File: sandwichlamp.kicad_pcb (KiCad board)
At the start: 2 copper layers, 96 x 96 mm, 17 parts, among them J1 Conn_01x01_Pin, J2 Conn_01x01_Pin, J3 Conn_01x01_Pin, J4 12V Enable, J5 HLK-LD2410C, J6 Conn_01x20_Pin, SW1 SW_SPDT, U1 magnetic-charger, U3 hw357, U4 RX480E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

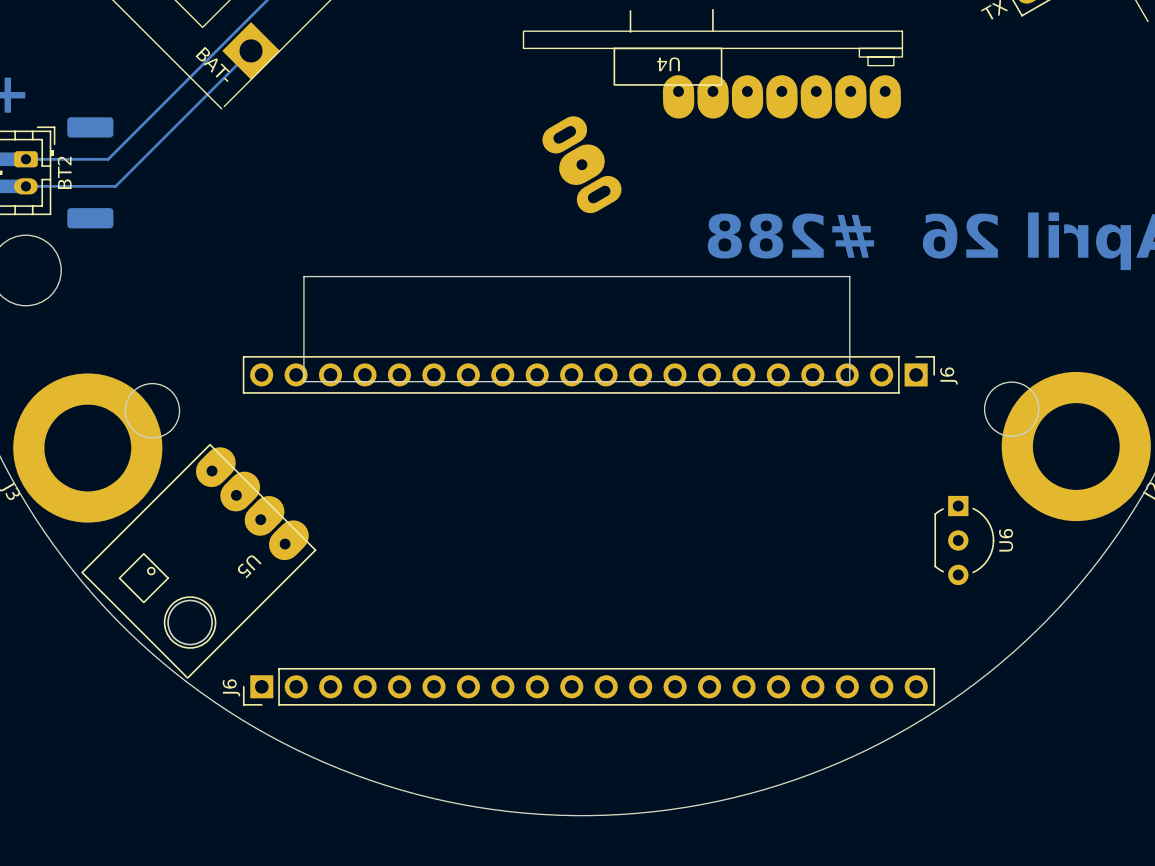
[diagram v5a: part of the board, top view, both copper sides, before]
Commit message: Add the new Lolin32 footprint
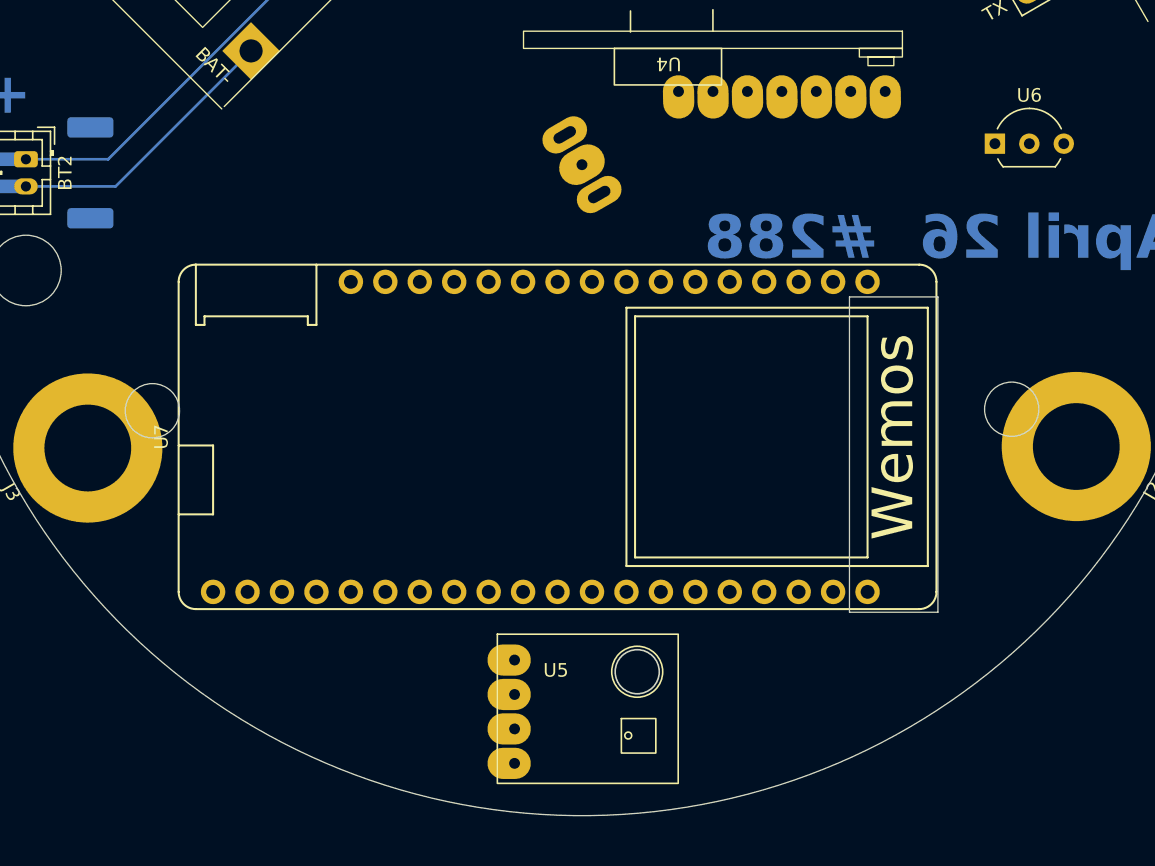
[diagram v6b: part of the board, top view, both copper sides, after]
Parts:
- removed J6 (x2): Conn_01x20_Pin, Connector_PinHeader_2.54mm:PinHeader_1x20_P2.54mm_Vertical
- added U7: Lolin32, lolin32:lolin32, F.Cu at (96.9, 120.1)
- moved U6 26.9 mm to (130.4, 98.5), turned to 0 degrees
- moved U5 24.7 mm to (95.0, 140.3), turned to 0 degrees
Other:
- outline, holes or cut-outs redrawn

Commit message: Update Lolin Footprint
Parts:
- moved U7 2.75 mm to (99.6, 119.6)
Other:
- outline, holes or cut-outs redrawn

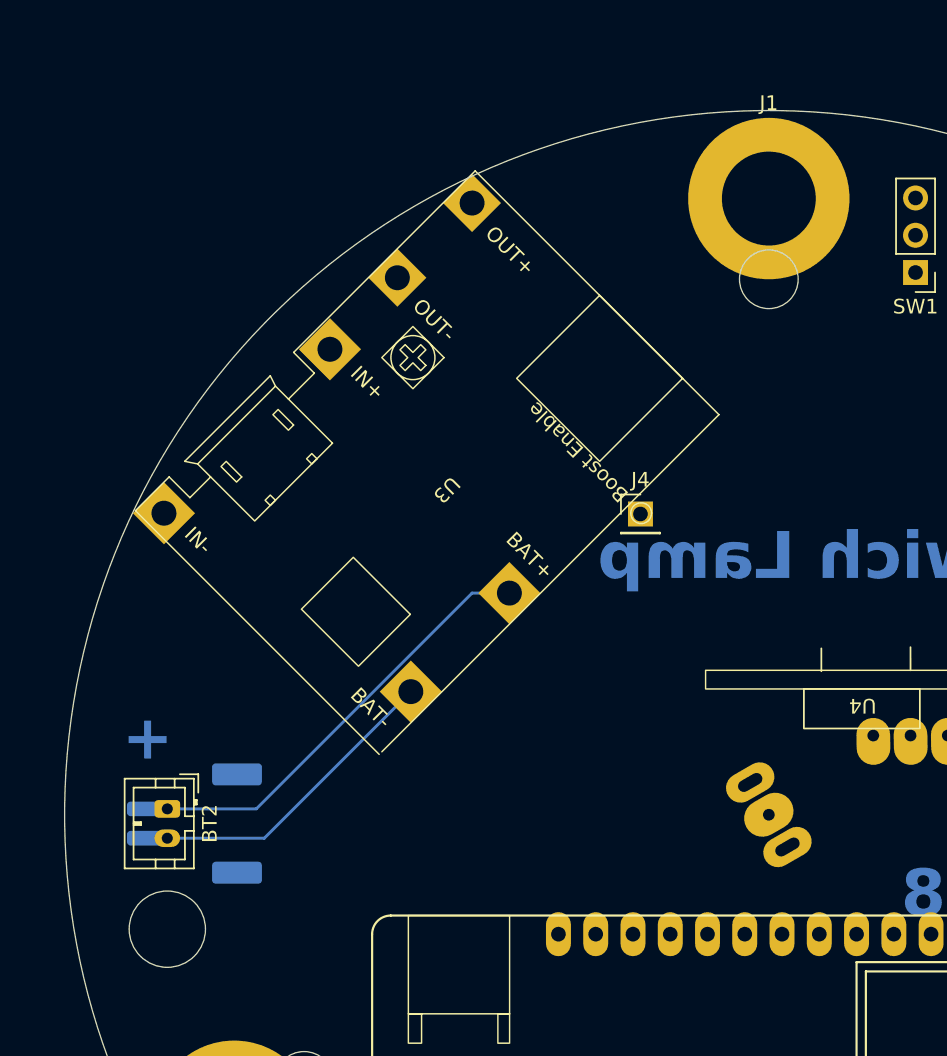
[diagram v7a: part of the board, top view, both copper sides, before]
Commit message: Add power switch and power switch for the radar
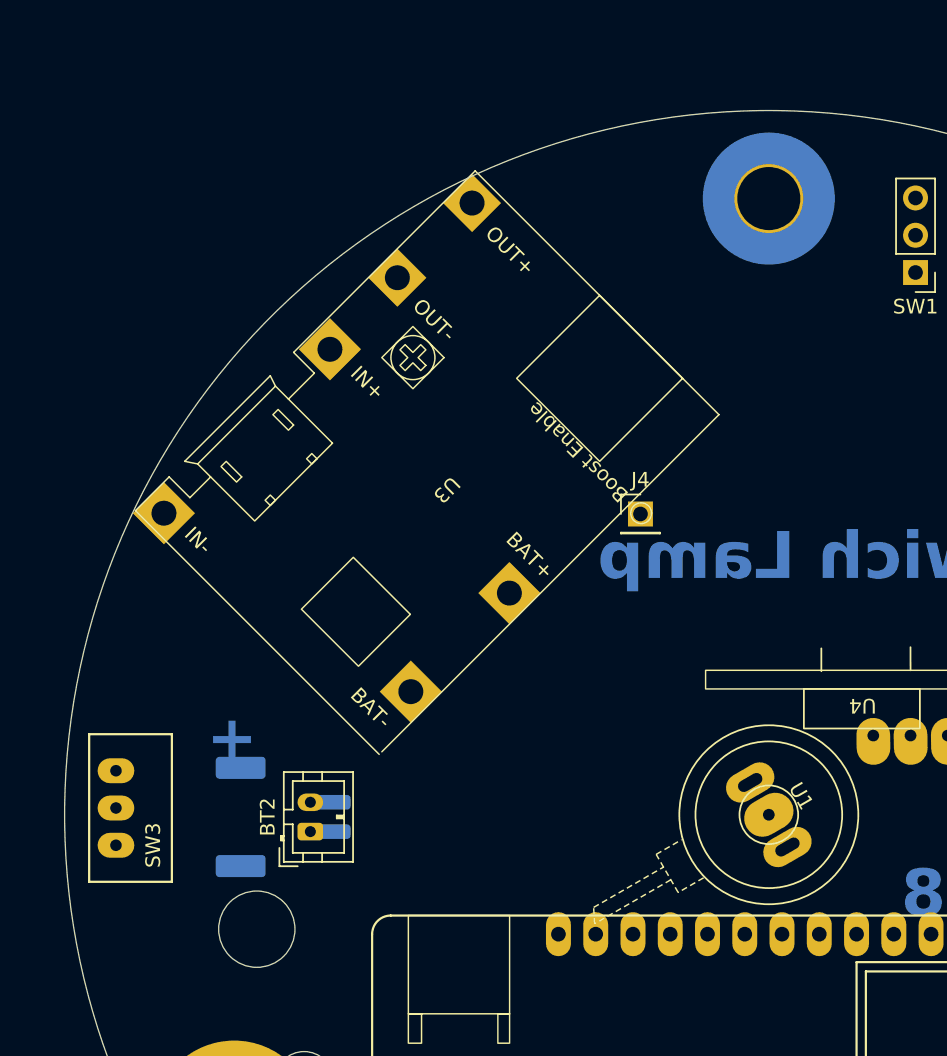
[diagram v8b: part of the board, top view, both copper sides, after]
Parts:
- added SW3: POWER, as12ap:as12ap, F.Cu at (55.5, 97.0)
- J1: value Conn_01x01_Pin -> Pole1; footprint MountingHole:MountingHole_6.4mm_M6_DIN965_Pad -> MountingHole:MountingHole_4.3mm_M4_ISO7380_Pad_TopOnly; moved to B.Cu
- J2: value Conn_01x01_Pin -> Pole2
- J3: value Conn_01x01_Pin -> Pole3
- SW1: value SW_SPDT -> Rader Power
- U1: moved to F.Cu
- moved BT2 9.87 mm to (68.8, 101.2), turned to 90 degrees
- moved BT1 6.07 mm to (66.9, 100.2), turned to 90 degrees
- turned J1 to 180 degrees
- turned U1 to -60 degrees
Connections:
- J5 pad 1: +5V -> Net-(J5-Pin_1)
- SW1 pad 1: unconnected-(SW1-A-Pad1) -> +5V
- SW1 pad 2: VBUS -> Net-(J5-Pin_1)
- SW1 pad 3: Net-(D2-K) -> +4V
- U7 pad 1: unconnected-(U7-3V3-Pad1) -> +3V3
- U7 pad 15: unconnected-(U7-5V-Pad15) -> VBUS
- U7 pad 16: unconnected-(U7-GND-Pad16) -> GND
- U7 pad 20: unconnected-(U7-3V3-Pad20) -> +3V3
- U7 pad 23: unconnected-(U7-GND-Pad23) -> GND
- U7 pad 24: unconnected-(U7-GND-Pad24) -> GND
- U7 pad 29: unconnected-(U7-3V3-Pad29) -> +3V3
- U7 pad 34: unconnected-(U7-GND-Pad34) -> GND
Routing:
- net +4V: track 29.4 -> 0.00 mm
- net GND: track 20.7 -> 0.00 mm
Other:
- outline, holes or cut-outs redrawn
